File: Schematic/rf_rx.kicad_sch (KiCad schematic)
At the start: 17 parts, among them J1 U.FL-R-SMT-1_01_, U1 ME6217C33M5G, U12 E28-2G4M27SX, U14 MIA-M10Q, U18 MAX40200ANS, Y2 CM8V-T1A

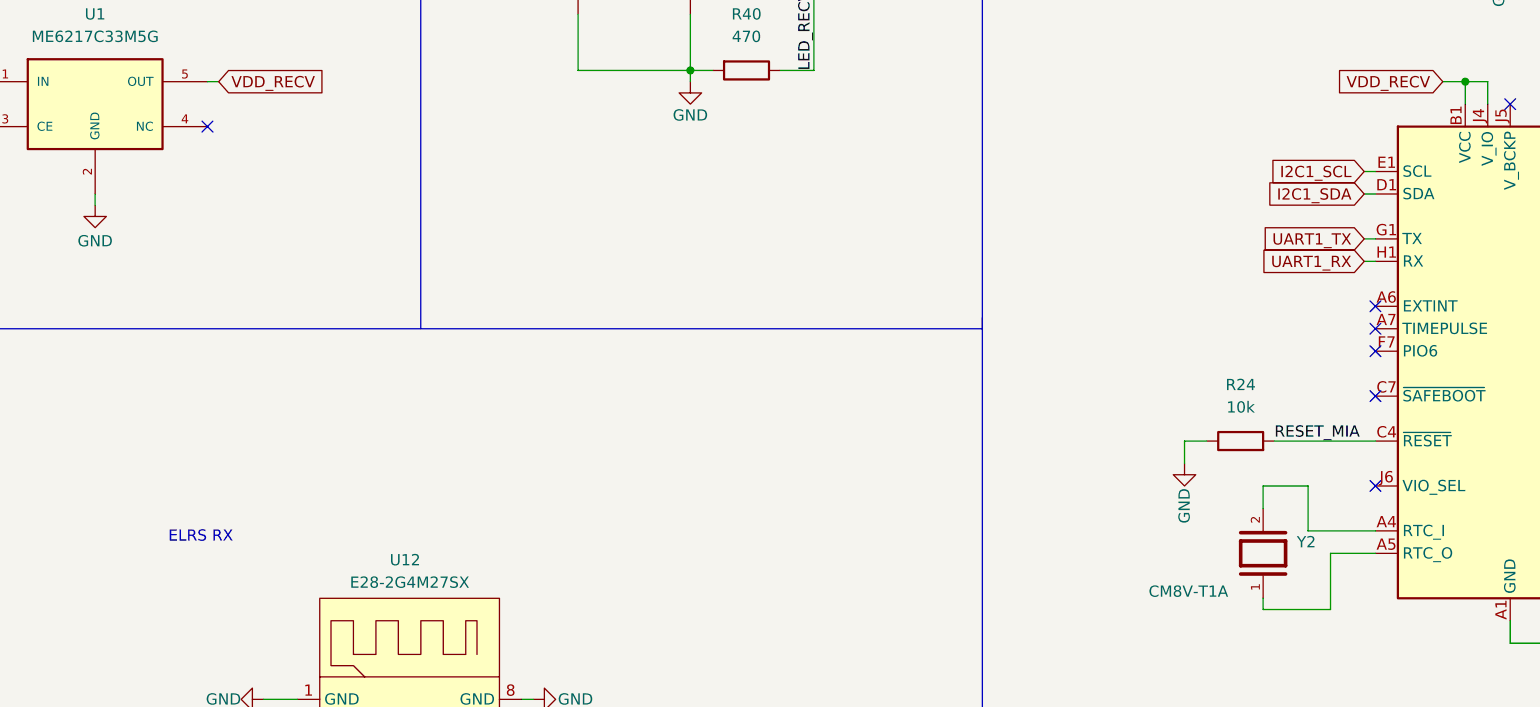
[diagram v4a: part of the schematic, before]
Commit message: update: refine component labels for IMU and Magnetometer in schematic
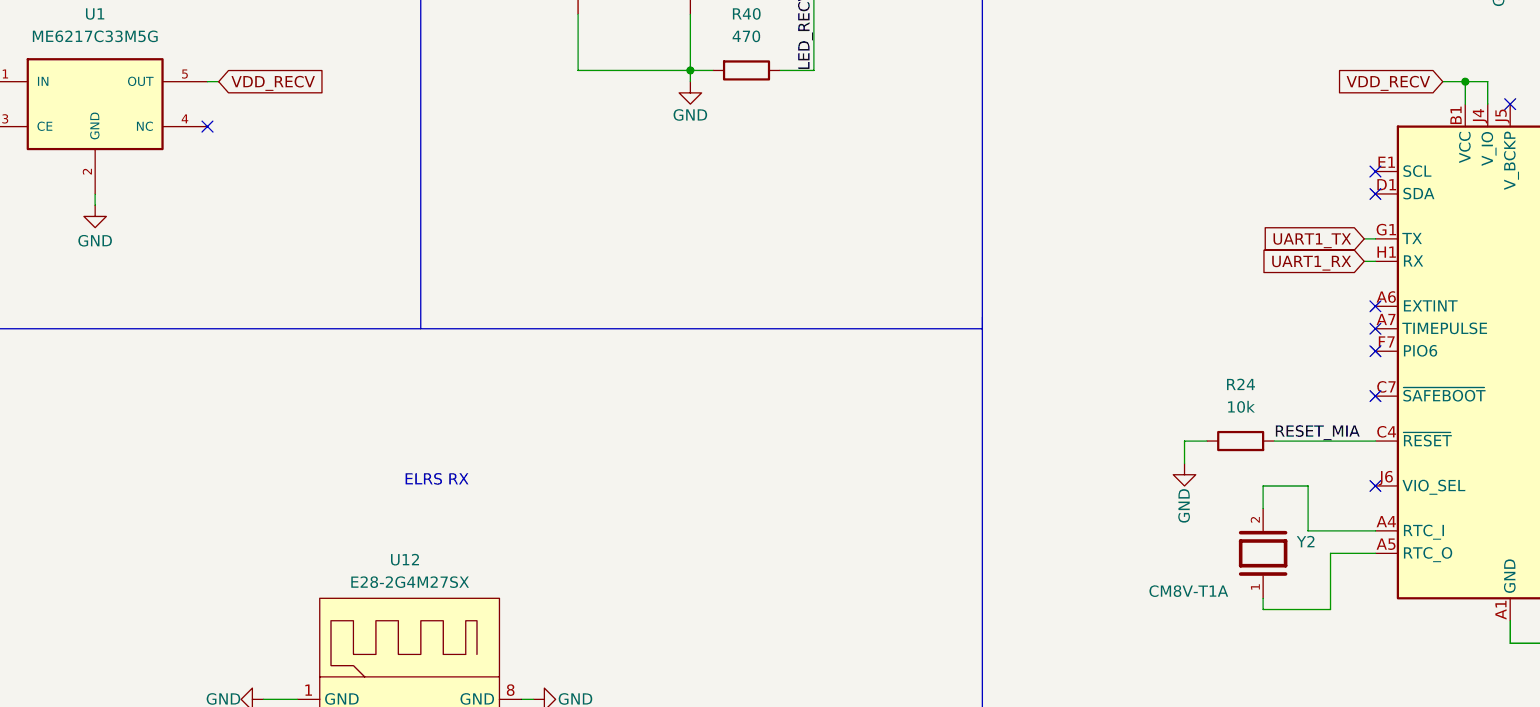
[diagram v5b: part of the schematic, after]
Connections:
- net I2C1_SCL: no longer names the net of U14.E1 (SCL)
- net I2C1_SDA: no longer names the net of U14.D1 (SDA)
- no-connect marks 13 -> 15
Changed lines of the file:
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@@
 	(text "ELRS RX "
 		(exclude_from_sim no)
-		(at 56.388 108.712 0)
+		(at 83.058 102.362 0)
 		(effects
 			(font
@@
 	)
 	(no_connect
+		(at 189.23 67.31)
+	)
+	(no_connect
+		(at 189.23 69.85)
+	)
+	(no_connect
 		(at 189.23 102.87)
 	)
@@
 	(wire
 		(pts
-			(xy 187.96 67.31) (xy 189.23 67.31)
-		)
-		(stroke
-			(width 0)
-			(type default)
-		)
-	)
-	(wire
-		(pts
 			(xy 236.22 29.21) (xy 240.03 29.21)
 		)
@@
 		(pts
 			(xy 240.03 38.1) (xy 240.03 39.37)
-		)
-		(stroke
-			(width 0)
-			(type default)
-		)
-	)
-	(wire
-		(pts
-			(xy 187.96 69.85) (xy 189.23 69.85)
 		)
 		(stroke
@@
 				(hide yes)
 			)
-		)
-	)
-	(global_label "I2C1_SDA"
-		(shape input)
-		(at 187.96 69.85 180)
-		(fields_autoplaced yes)
-		(effects
-			(font
-				(size 1.27 1.27)
-			)
-			(justify right)
-		)
-		(property "Intersheetrefs" "${INTERSHEET_REFS}"
-			(at 176.1453 69.85 0)
-			(effects
-				(font
-					(size 1.27 1.27)
-				)
-				(justify right)
-				(hide yes)
-			)
-		)
-	)
-	(global_label "I2C1_SCL"
-		(shape input)
-		(at 187.96 67.31 180)
-		(fields_autoplaced yes)
-		(effects
-			(font
-				(size 1.27 1.27)
-			)
-			(justify right)
-		)
-		(property "Intersheetrefs" "${INTERSHEET_REFS}"
-			(at 176.2058 67.31 0)
-			(effects
-				(font
-					(size 1.27 1.27)
-				)
-				(justify right)
-				(hide yes)
-			)
